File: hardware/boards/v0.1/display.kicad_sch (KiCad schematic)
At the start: 14 parts, among them U19 ER-TFT024IPS-3, U26 ER-TFT028A-4

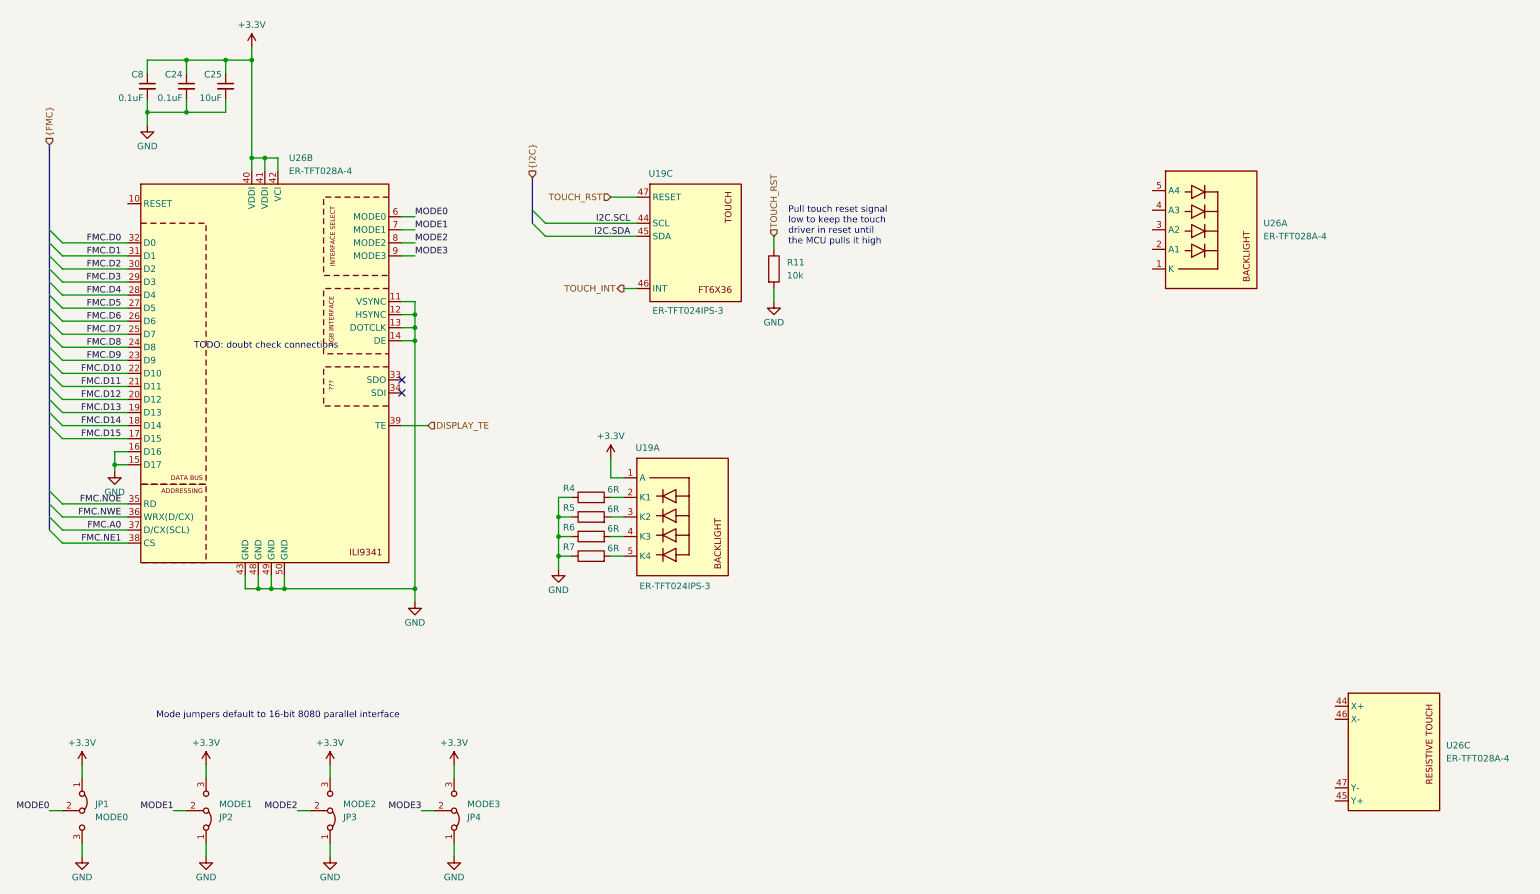
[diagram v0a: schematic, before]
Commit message: feat: various component and layout changes
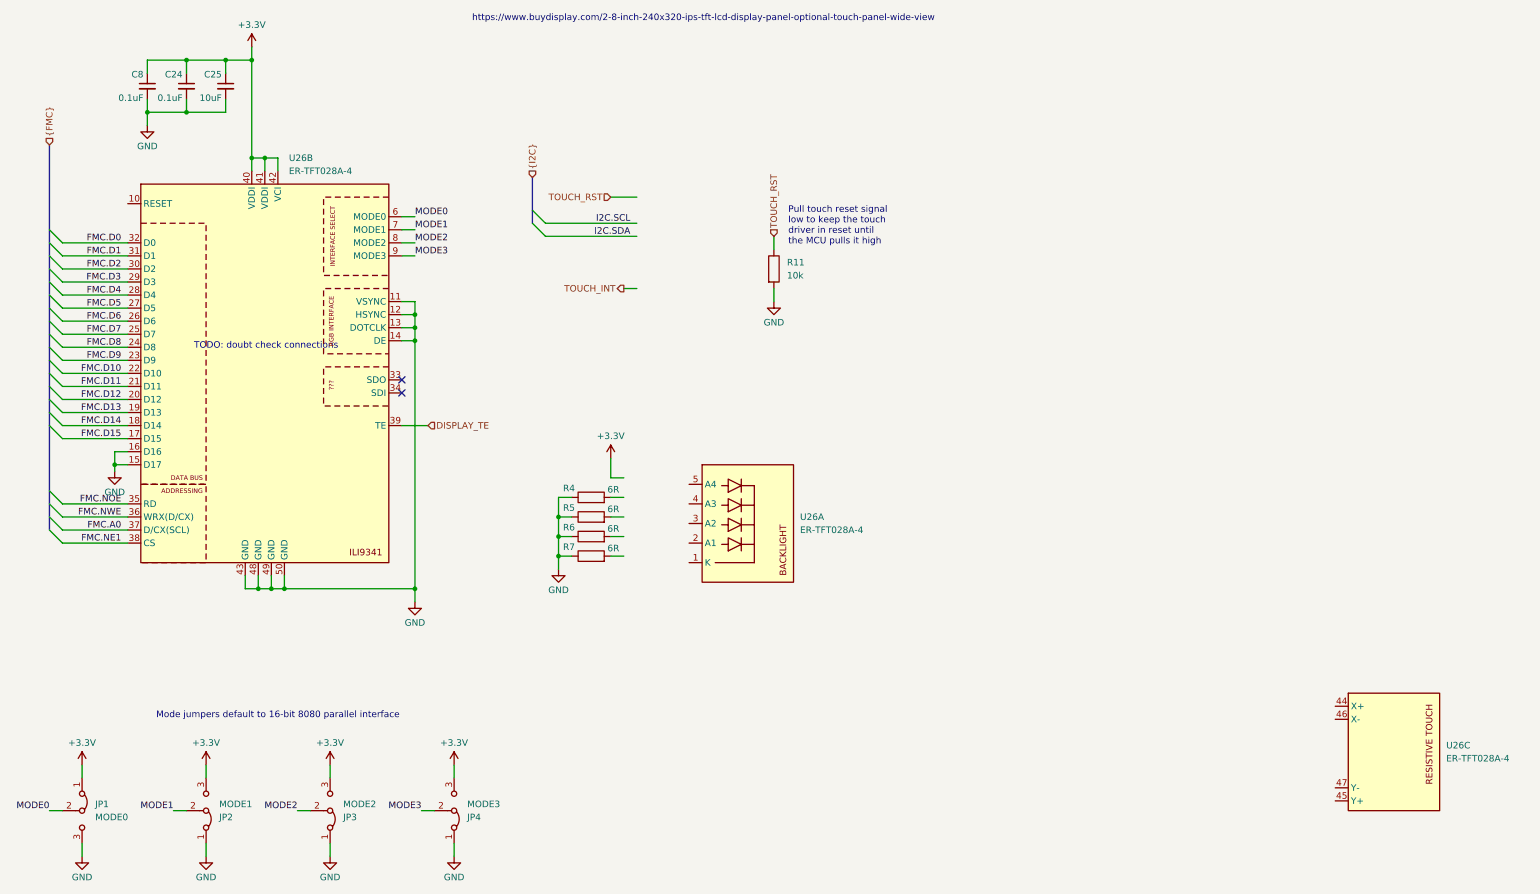
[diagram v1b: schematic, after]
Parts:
- removed U19: ER-TFT024IPS-3, pocket_synth:ER-TFT024IPS-3, symbol pocket_synth:ER-TFT024IPS-3
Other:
- note added: "https://www.buydisplay.com/2-8-inch-240x320-ips-tft-lcd-display-panel-optional-touch-panel-wide-view"
- moved on the sheet: U26A

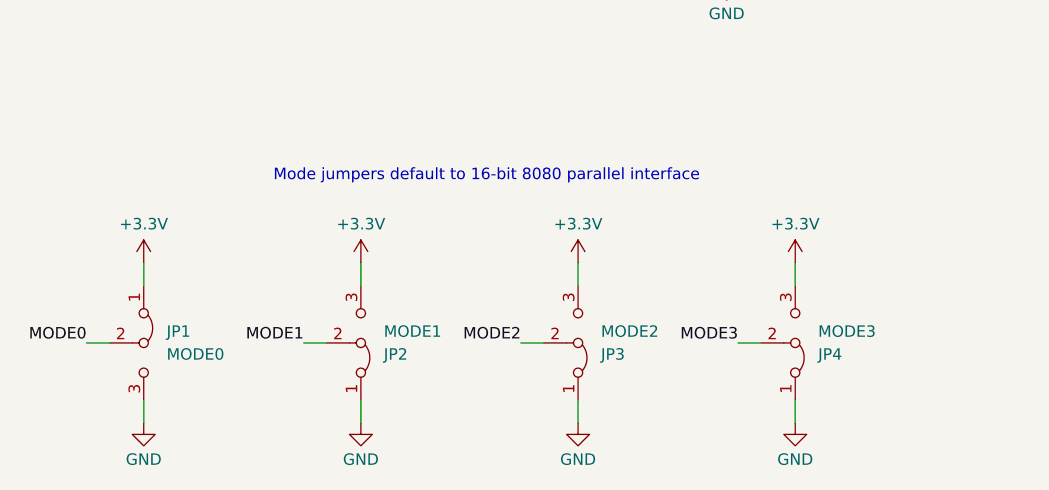
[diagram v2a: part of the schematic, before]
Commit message: feat: route audio components
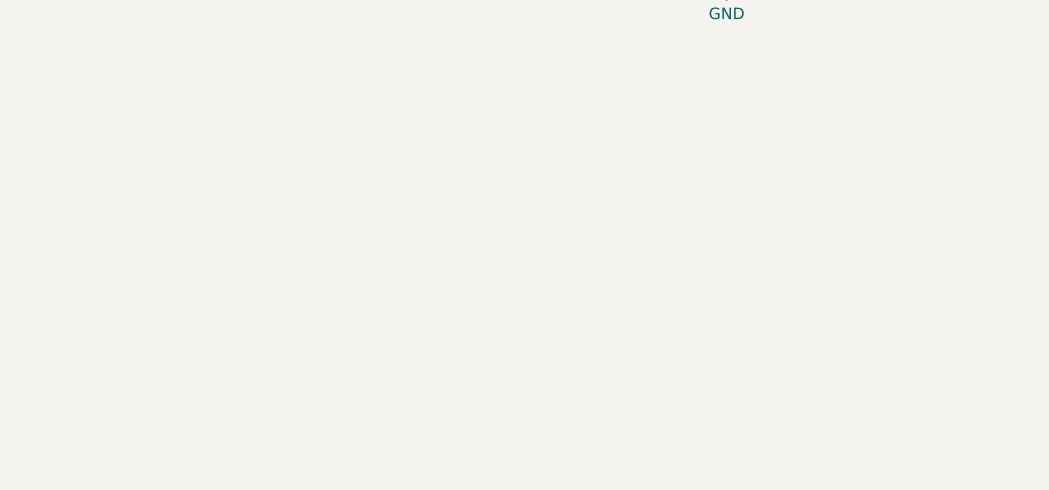
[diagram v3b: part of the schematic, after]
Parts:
- removed JP1: MODE0, Jumper:SolderJumper-3_P1.3mm_Bridged12_RoundedPad1.0x1.5mm, symbol Jumper:Jumper_3_Bridged12
- removed JP2: MODE1, Jumper:SolderJumper-3_P1.3mm_Bridged12_RoundedPad1.0x1.5mm, symbol Jumper:Jumper_3_Bridged12
- removed JP3: MODE2, Jumper:SolderJumper-3_P1.3mm_Bridged12_RoundedPad1.0x1.5mm, symbol Jumper:Jumper_3_Bridged12
- removed JP4: MODE3, Jumper:SolderJumper-3_P1.3mm_Bridged12_RoundedPad1.0x1.5mm, symbol Jumper:Jumper_3_Bridged12
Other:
- note removed: "Mode jumpers default to 16-bit 8080 parallel interface"

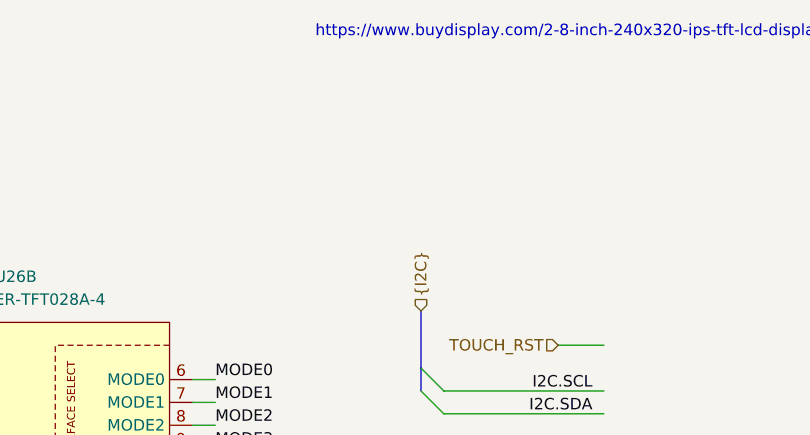
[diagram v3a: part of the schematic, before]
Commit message: feat: schematic organization and ERC cleanup
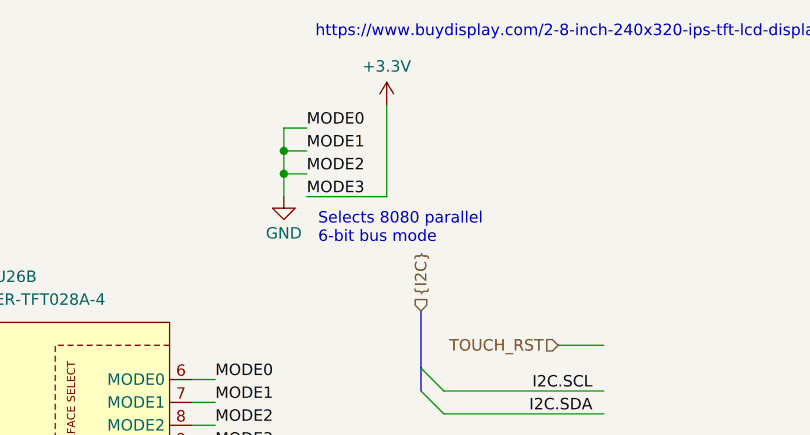
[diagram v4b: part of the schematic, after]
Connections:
- net MODE0 is gone; now on net GND: U26.6 (MODE0)
- net MODE1 is gone; now on net GND: U26.7 (MODE1)
- net MODE2 is gone; now on net GND: U26.8 (MODE2)
- net MODE3 is gone; now on net +3.3V: U26.9 (MODE3)
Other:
- note added: "Selects 8080 parallel 6-bit bus mode"

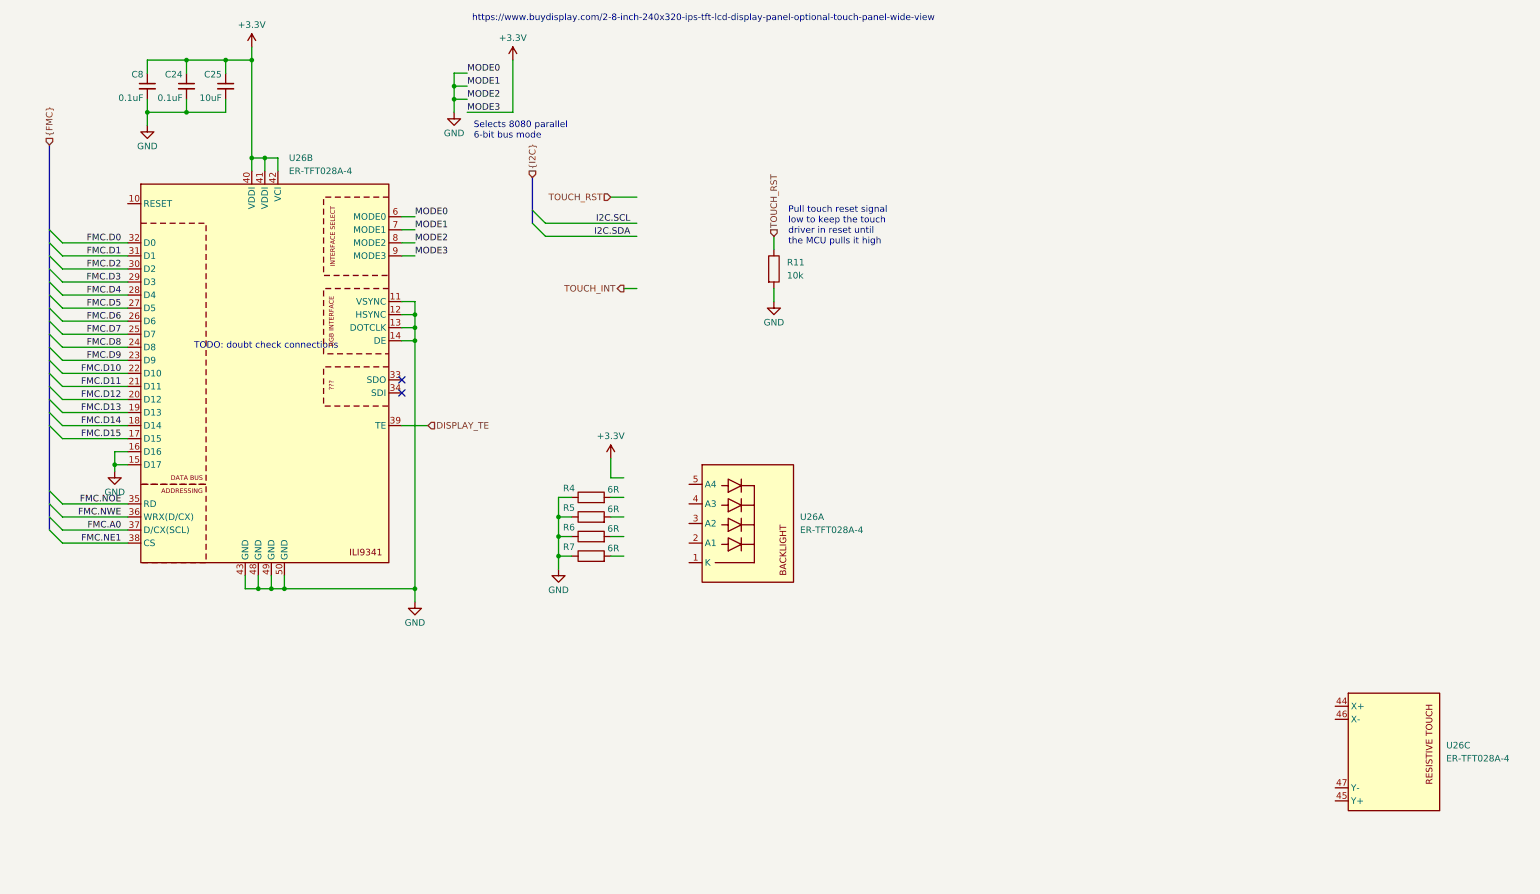
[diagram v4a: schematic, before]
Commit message: feat: add touch screen connector, input I2C bus
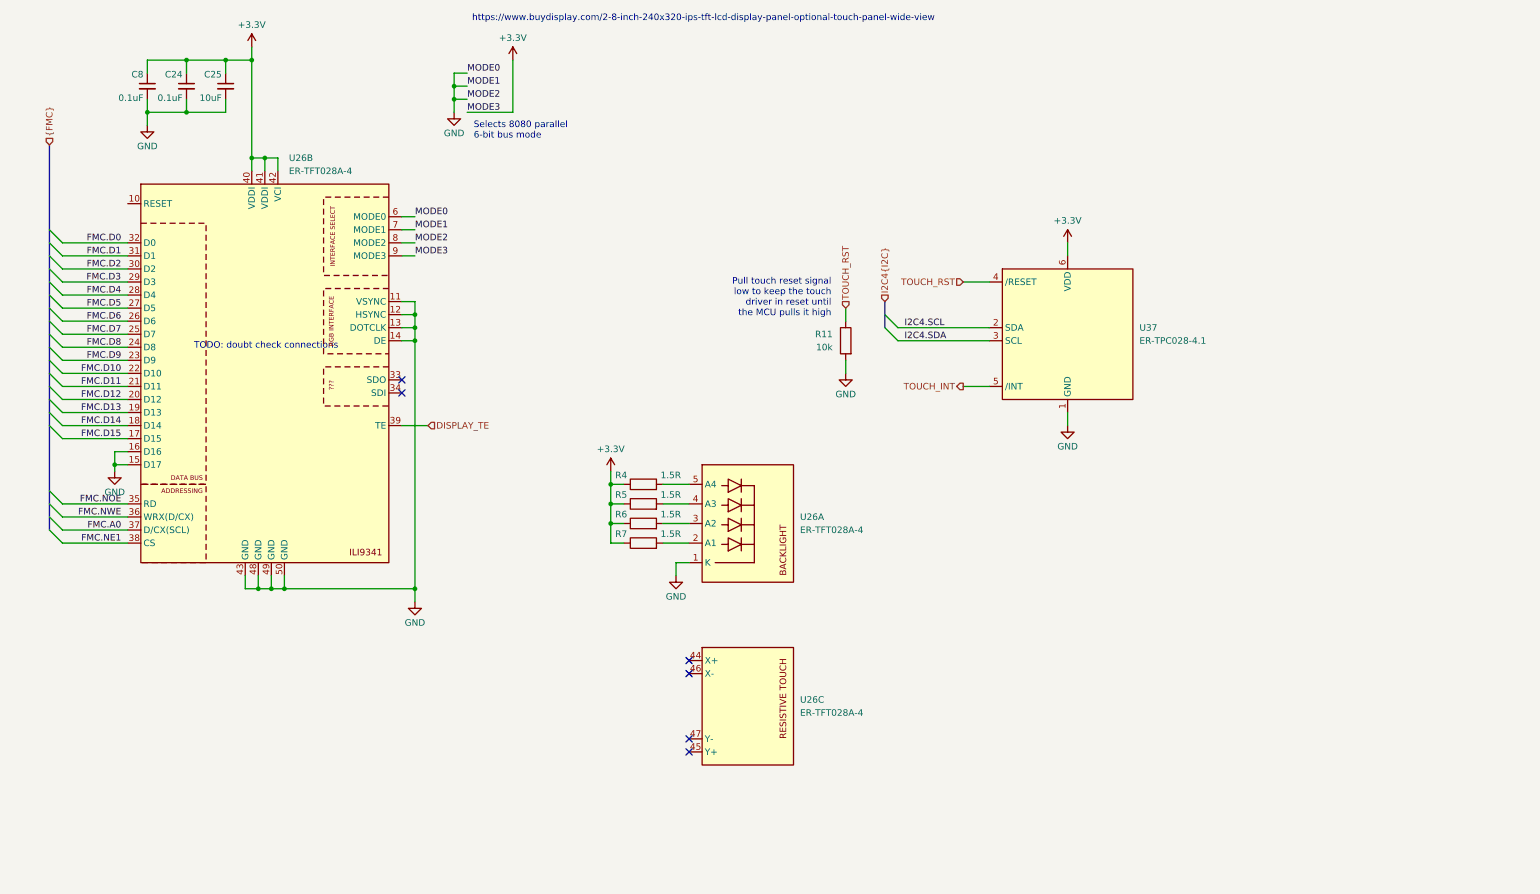
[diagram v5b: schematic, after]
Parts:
- added U37: ER-TPC028-4.1, pocket_synth:ER-CON06HB-1, symbol pocket_synth:ER-TPC028-4.1
- R4, R5, R6, R7: value 6R -> 1.5R
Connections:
- net +3.3V: now also R4.1, R5.1, R6.1, R7.1, U37.6 (VDD)
- net GND: now also U26.1 (K), U37.1 (GND); no longer R4.1, R5.1, R6.1, R7.1
- net TOUCH_INT: now also U37.5 (/INT)
- net TOUCH_RST: now also U37.4 (/RESET)
- net at R5.2: now also U26.4 (A3)
- net at R4.2: now also U26.5 (A4)
- net at R6.2: now also U26.3 (A2)
- net at R7.2: now also U26.2 (A1)
- new net I2C4.SCL: U37.2 (SDA)
- new net I2C4.SDA: U37.3 (SCL)
- no-connect marks 2 -> 6
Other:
- moved on the sheet: R11, R4, R5, R6, R7, U26C

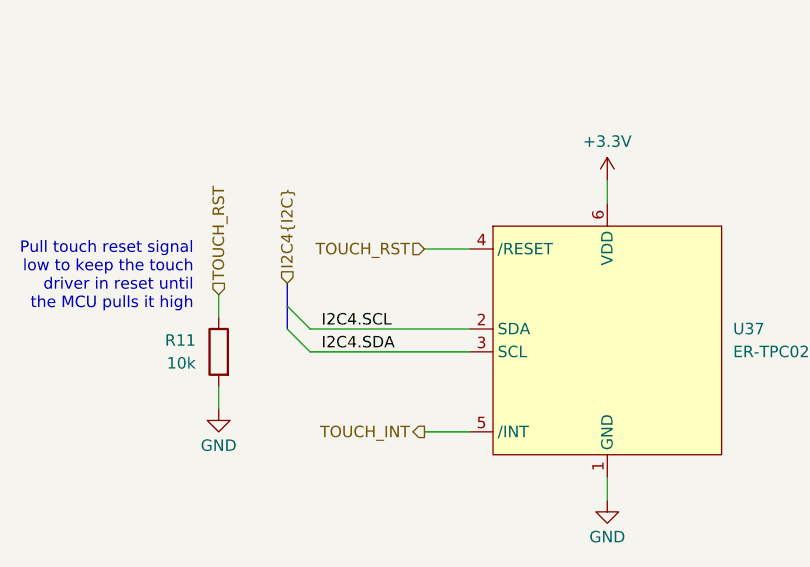
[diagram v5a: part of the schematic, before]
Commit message: feat: various ERC and DRC cleanup
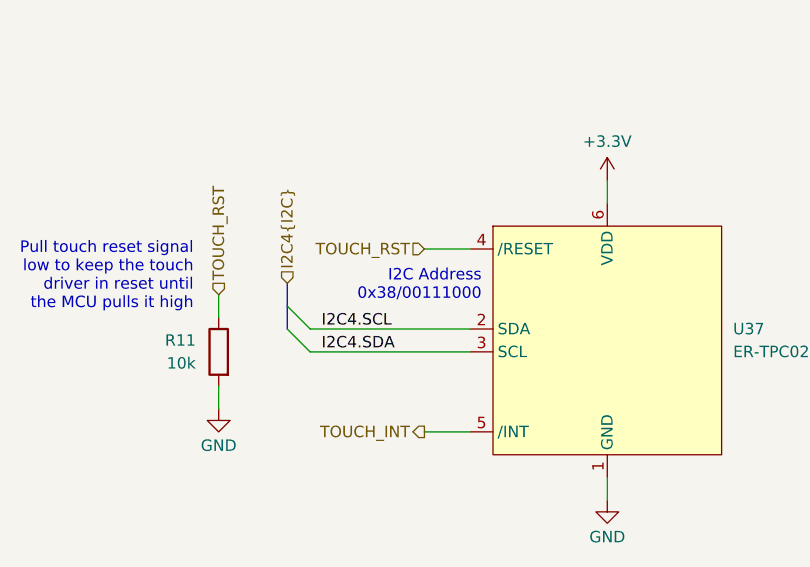
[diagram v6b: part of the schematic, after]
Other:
- note added: "I2C Address 0x38/00111000"
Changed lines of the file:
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@@
+		)
+	)
+	(text "I2C Address\n0x38/00111000"
+		(exclude_from_sim no)
+		(at 208.28 75.184 0)
+		(effects
+			(font
+				(size 1.27 1.27)
+				(color 132 132 132 1)
+			)
+			(justify right)
 		)
 	)

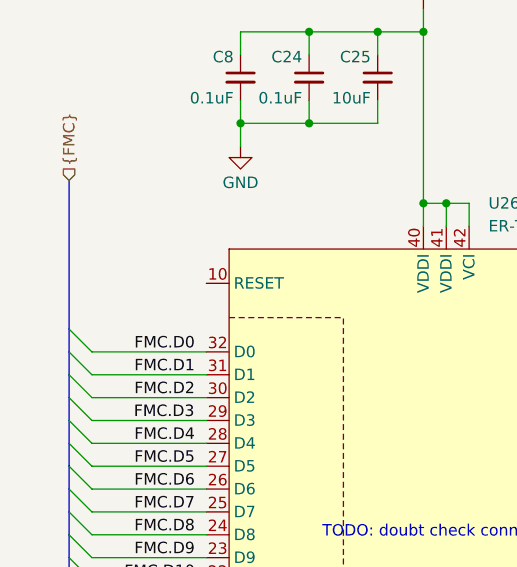
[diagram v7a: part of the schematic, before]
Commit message: feat: add display reset connection
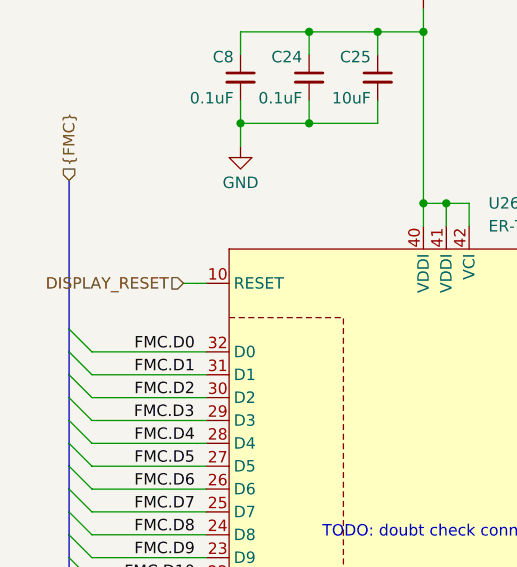
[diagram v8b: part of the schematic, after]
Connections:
- net DISPLAY_RESET: now reaches U26.10 (RESET)
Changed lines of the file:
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@@
+	(wire
+		(pts
+			(xy 36.83 55.88) (xy 39.37 55.88)
+		)
+		(stroke
+			(width 0)
+			(type default)
+		)
+	)
 	(wire
 		(pts
@@
 		)
 	)
+	(hierarchical_label "DISPLAY_RESET"
+		(shape input)
+		(at 36.83 55.88 180)
+		(effects
+			(font
+				(size 1.27 1.27)
+			)
+			(justify right)
+		)
+	)
